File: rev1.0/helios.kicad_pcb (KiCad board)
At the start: 4 copper layers, 17.8 x 33 mm, 58 parts, among them J1 USB_C_Receptacle_USB2.0, J2 helios-pinout, Q1 2N7002VC-, Q2 2N7002VC-, SW1 SWITCH, U1 USBLC6-2P6, U2 LP5907SNX-3.3-NOPB, U3 W25Q128JVPIQ, U4 RP2040, U5 74LVC1T45, Y1 12MHz

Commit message: updated assembly files again
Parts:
- moved R13 0.42 mm to (160.1, 143.8)
- moved R12 0.41 mm to (157.6, 143.8)
- moved JP1 0.28 mm to (153.4, 145.6)
- moved R9 0.20 mm to (155.3, 144.7)
- moved SW1 0.18 mm to (164.5, 161.6)
- moved R11 0.17 mm to (154.8, 146.2)
- moved C16 0.16 mm to (155.5, 150.9)
- moved R2 0.16 mm to (156.8, 143.8)
- moved C10 0.11 mm to (160.4, 150.9)
- moved C14 0.11 mm to (159.3, 150.9)
- moved C17 0.11 mm to (158.4, 150.9)
- moved C18 0.11 mm to (162.2, 150.9)
- moved C9 0.11 mm to (161.3, 150.9)
- moved U1 0.08 mm to (158.9, 143.8)
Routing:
- net GND: track 7.69 -> 8.81 mm, vias 38 -> 39
- net /23_SDO: track 8.66 -> 9.75 mm, vias 0 -> 1
- net /D-: track 12.0 -> 12.6 mm
- net /D+: track 12.0 -> 12.6 mm
- net /1_RX0: track 16.4 -> 16.3 mm, vias 1 -> 0

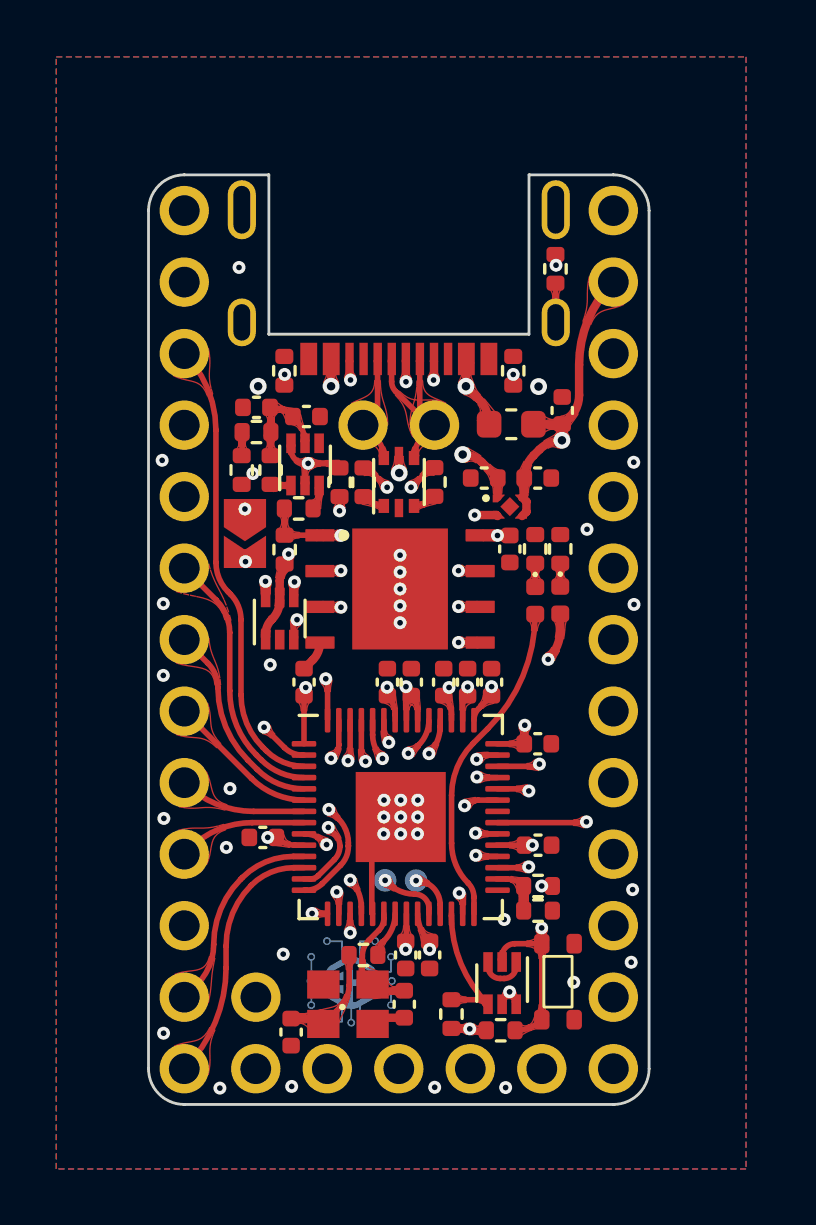
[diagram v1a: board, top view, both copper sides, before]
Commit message: fixed proto mistakes, revised power circuit and added option to use vbus on the 5v pin
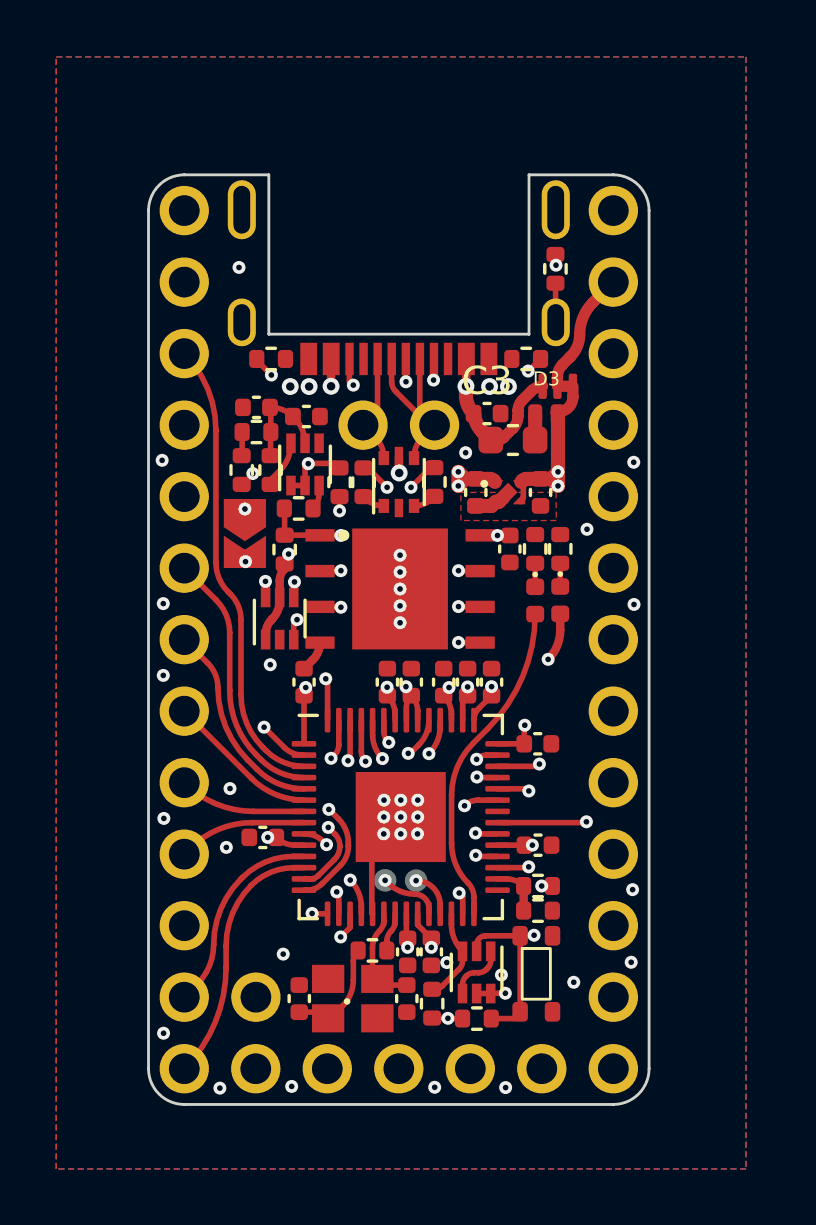
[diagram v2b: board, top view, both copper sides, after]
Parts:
- removed the REF** at (158.8, 160.0)
- added D3: PMEG2010BELD, 0xcb:SOD882D, F.Cu at (164.1, 141.4)
- added JP2: Jumper_3_Bridged12, 0xcb:SolderJumper-3_P1.3mm_Bridged12_RoundedPad1.0x1.5mm_NumberLabels, F.Cu at (164.5, 140.4)
- U2: value LP5907SNX-3.3-NOPB -> TLV75533PDQNR
- moved C3 2.67 mm to (162.0, 141.4), turned to 0 degrees
- moved C8 1.22 mm to (155.3, 162.2), turned to -90 degrees
- moved Q1 0.98 mm to (161.6, 161.2)
- moved R1 0.94 mm to (161.6, 162.9)
- moved SW1 0.82 mm to (163.7, 161.3)
- moved R3 0.78 mm to (160.0, 162.3)
- moved R8 0.63 mm to (154.3, 139.4), turned to 180 degrees
- moved R7 0.62 mm to (163.4, 139.4), turned to 0 degrees
- moved C5 0.59 mm to (161.6, 144.2), turned to -90 degrees
- moved F1 0.56 mm to (162.9, 142.3)
- moved C4 0.52 mm to (163.9, 144.2), turned to -90 degrees
- moved U2 0.51 mm to (162.7, 144.2)
- moved R14 0.36 mm to (157.9, 160.4)
- moved Y1 0.26 mm to (157.2, 162.2)
- moved C7 0.22 mm to (159.1, 162.2)
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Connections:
- C3 pad 1: +5V -> VBUS
- F1 pad 2: +5V -> Net-(D3-Pad2)
- J2 pad 30: +5V -> /RAW
- Q1 pad 3: GND -> /RST
- Q1 pad 4: /RST -> GND
- Q2 pad 1: Net-(Q2-Pad1) -> Net-(Q1-Pad5)
- Q2 pad 6: Net-(Q1-Pad5) -> Net-(Q2-Pad6)
- R4 pad 1: Net-(Q2-Pad1) -> Net-(Q2-Pad6)
- U2 pad 5: unconnected-(U2-Pad5) -> GND
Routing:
- net /RAW: track 0.00 -> 4.36 mm
- net +5V: track 25.0 -> 20.9 mm, vias 3 -> 4
- net VBUS: track 28.5 -> 32.0 mm
- net Net-(Q1-Pad5): track 28.3 -> 26.5 mm
- net Net-(Q2-Pad6): track 0.00 -> 1.69 mm
- net /RST: track 4.88 -> 3.33 mm
- net Net-(J1-PadB5): track 3.61 -> 4.91 mm
- net Net-(D3-Pad2): track 0.00 -> 0.92 mm
- net Net-(Q2-Pad1): track 0.74 -> 0.00 mm
- net Net-(J1-PadA5): track 4.09 -> 4.82 mm
- net GND: track 8.81 -> 8.22 mm, vias 39 -> 42
- net Net-(C7-Pad2): track 4.10 -> 3.60 mm
- net +3V3: track 20.5 -> 20.6 mm, vias 15 -> 16

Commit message: prod files
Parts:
- added REF**: LOGO, art:LOGO, B.Cu at (158.9, 162.2)
- moved D2 2.97 mm to (163.0, 150.9)
- moved D1 2.97 mm to (163.9, 150.9)
- moved R10 2.97 mm to (163.9, 149.1)
- moved R15 2.97 mm to (163.0, 149.1)
- moved C6 0.83 mm to (163.5, 145.7), turned to 0 degrees
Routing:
- net /LED: track 11.7 -> 8.77 mm
- net Net-(D1-Pad2): track 24.1 -> 22.3 mm
- net +3V3: track 20.6 -> 21.3 mm, vias 16 -> 15
- net GND: vias 42 -> 45

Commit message: production files
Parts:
- C1, C10, C11, C12, C13, C14, C15, C16, C17, C18, C19, C2, C3, C4, C5, C6, C7, C8, C9: footprint Capacitor_SMD:C_0402_1005Metric -> 0xcb:C_0402_1005Metric
- D1, D2: footprint Diode_SMD:D_0402_1005Metric -> 0xcb:D_0402_1005Metric
- F1: footprint Fuse:Fuse_0603_1608Metric -> 0xcb:Fuse_0603_1608Metric
- FB1, R1, R10, R11, R12, R13, R14, R15, R16, R17, R2, R3, R4, R5, R6, R7, R8, R9: footprint Resistor_SMD:R_0402_1005Metric -> 0xcb:R_0402_1005Metric
- Q1, Q2, U5: footprint Package_TO_SOT_SMD:SOT-563 -> 0xcb:SOT-563
- U1: footprint Package_TO_SOT_SMD:SOT-666 -> 0xcb:SOT-666
- U4: footprint Package_DFN_QFN:QFN-56-1EP_7x7mm_P0.4mm_EP3.2x3.2mm -> 0xcb:QFN-56-1EP_7x7mm_P0.4mm_EP3.2x3.2mm
- Y1: footprint Crystal:Crystal_SMD_2520-4Pin_2.5x2.0mm -> 0xcb:Crystal_SMD_2520-4Pin_2.5x2.0mm

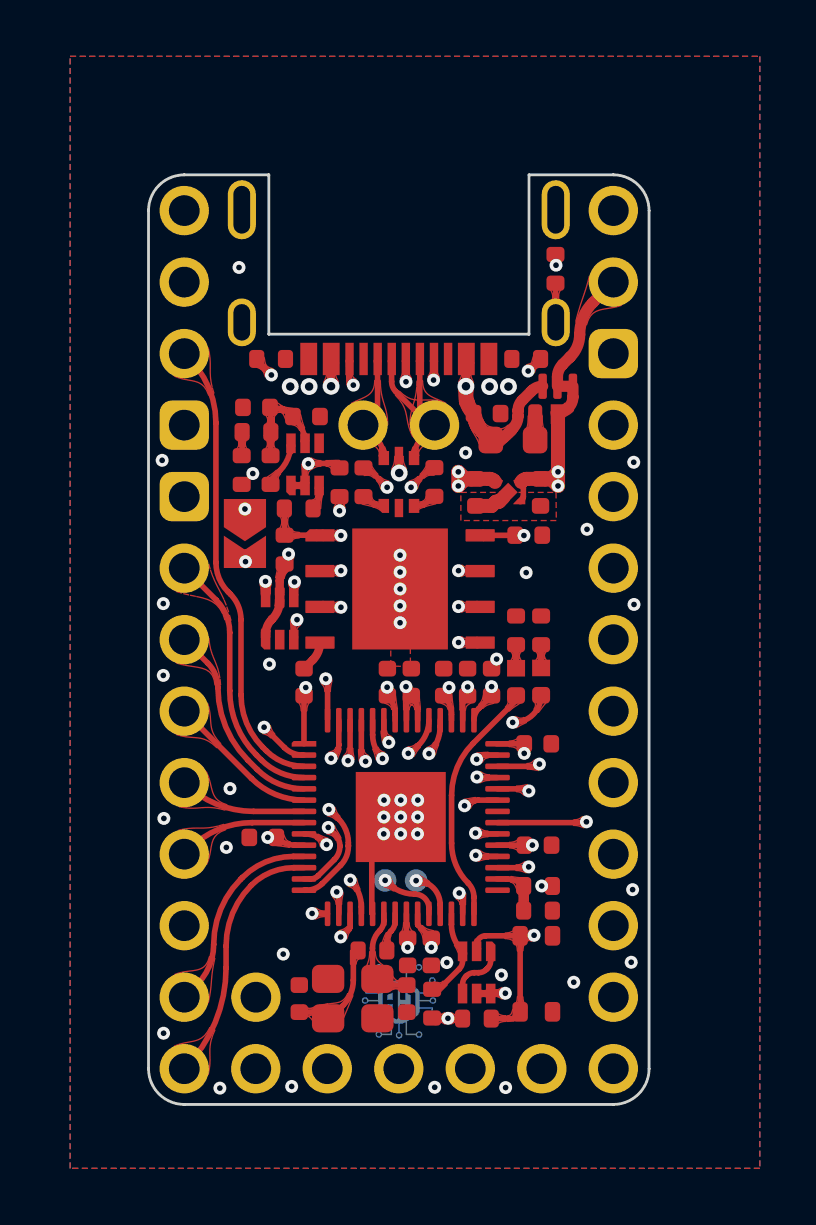
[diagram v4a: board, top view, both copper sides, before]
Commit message: add castellated holes
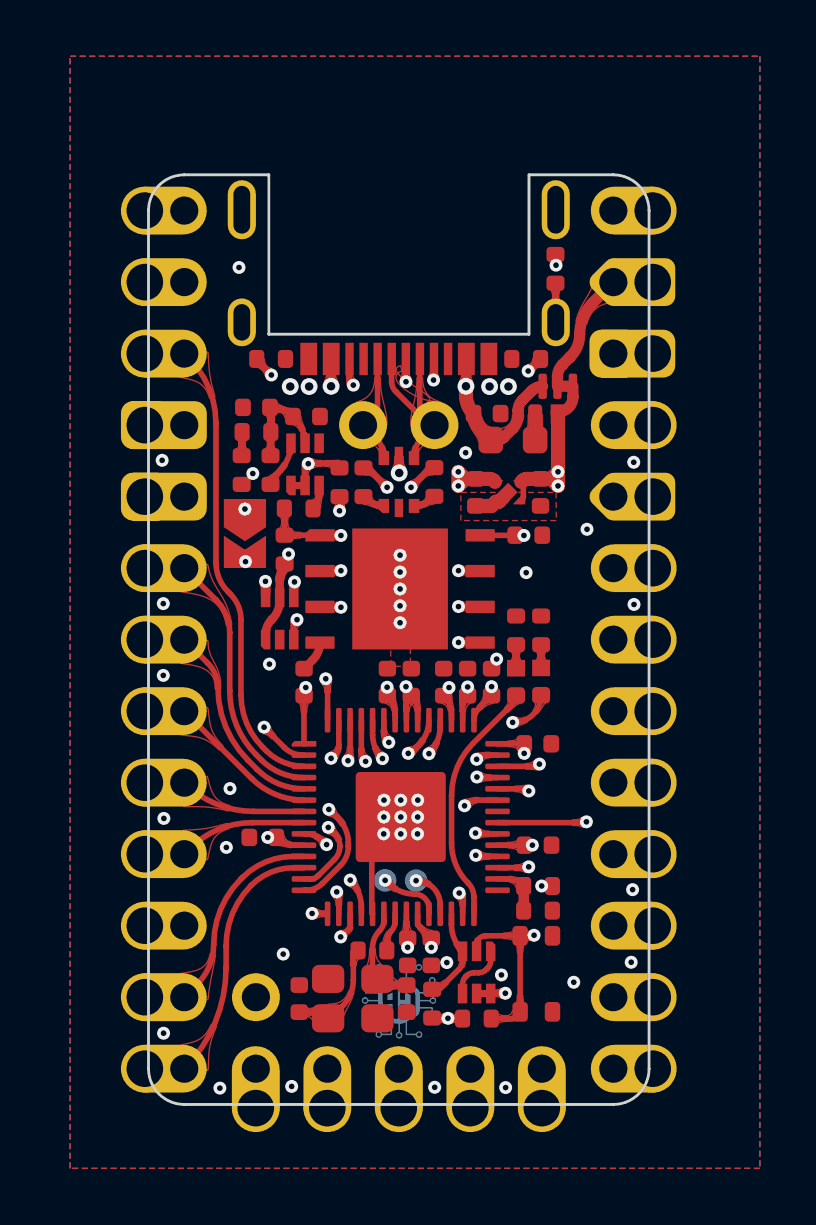
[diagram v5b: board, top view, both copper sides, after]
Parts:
- U4: footprint 0xcb:QFN-56-1EP_7x7mm_P0.4mm_EP3.2x3.2mm -> 0xcb:RP2040-QFN-56

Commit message: fix tabs in pads
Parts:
- removed the REF** at (158.9, 166.3)
- added REF**: Tab, kikit:Tab, F.Cu at (165.7, 166.4)
- added REF**: Tab, kikit:Tab, F.Cu at (152.0, 166.4)
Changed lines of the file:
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@@
+      (stroke (width 0.3) (type solid)) (layer "Dwgs.User"))
+  )
+  (footprint "kikit:Tab" (layer "F.Cu")
+    (at 165.73 166.36 90)
+    (descr "A symbol representing annotation for tab placement")
+    (attr board_only exclude_from_pos_files exclude_from_bom)
+    (fp_text reference "REF**" (at 0 -2 90) (layer "F.SilkS") hide
+        (effects (font (size 1 1) (thickness 0.15)))
+    )
+    (fp_text value "Tab" (at -2.75 -1 90) (layer "Dwgs.User")
+        (effects (font (size 1.2 1.2) (thickness 0.2)))
+    )
+    (fp_text user "KIKIT: width: 1.5mm" (at -5.5 0) (layer "Dwgs.User")
+        (effects (font (size 1 1) (thickness 0.15)))
+    )
+    (fp_line (start 0.25 0) (end -2.75 0)
+      (stroke (width 0.3) (type solid)) (layer "Dwgs.User"))
+    (fp_line (start 0.25 0) (end -0.75 -1)
+      (stroke (width 0.3) (type solid)) (layer "Dwgs.User"))
+    (fp_line (start 0.25 0) (end -0.75 1)
+      (stroke (width 0.3) (type solid)) (layer "Dwgs.User"))
+    (fp_line (start 0.25 1) (end 0.25 -1)
       (stroke (width 0.3) (type solid)) (layer "Dwgs.User"))
   )
@@
       (rotate (xyz 0 0 0))
     )
-  )
-  (footprint "kikit:Tab" (layer "F.Cu")
-    (at 158.9 166.26 90)
-    (descr "A symbol representing annotation for tab placement")
-    (attr board_only exclude_from_pos_files exclude_from_bom)
-    (fp_text reference "REF**" (at 0 -2 90) (layer "F.SilkS") hide
-        (effects (font (size 1 1) (thickness 0.15)))
-    )
-    (fp_text value "Tab" (at -2.75 -1 90) (layer "Dwgs.User")
-        (effects (font (size 1.2 1.2) (thickness 0.2)))
-    )
-    (fp_text user "KIKIT: width: 6mm" (at -5.5 0) (layer "Dwgs.User")
-        (effects (font (size 1 1) (thickness 0.15)))
-    )
-    (fp_line (start 0.25 0) (end -2.75 0)
-      (stroke (width 0.3) (type solid)) (layer "Dwgs.User"))
-    (fp_line (start 0.25 0) (end -0.75 -1)
-      (stroke (width 0.3) (type solid)) (layer "Dwgs.User"))
-    (fp_line (start 0.25 0) (end -0.75 1)
-      (stroke (width 0.3) (type solid)) (layer "Dwgs.User"))
-    (fp_line (start 0.25 1) (end 0.25 -1)
-      (stroke (width 0.3) (type solid)) (layer "Dwgs.User"))
   )
   (footprint "0xcb:C_0402_1005Metric" (layer "F.Cu")
@@
     )
   )
+  (footprint "kikit:Tab" (layer "F.Cu")
+    (at 151.98 166.36 90)
+    (descr "A symbol representing annotation for tab placement")
+    (attr board_only exclude_from_pos_files exclude_from_bom)
+    (fp_text reference "REF**" (at 0 -2 90) (layer "F.SilkS") hide
+        (effects (font (size 1 1) (thickness 0.15)))
+    )
+    (fp_text value "Tab" (at -2.75 -1 90) (layer "Dwgs.User")
+        (effects (font (size 1.2 1.2) (thickness 0.2)))
+    )
+    (fp_text user "KIKIT: width: 1.5mm" (at -5.5 0) (layer "Dwgs.User")
+        (effects (font (size 1 1) (thickness 0.15)))
+    )
+    (fp_line (start 0.25 0) (end -2.75 0)
+      (stroke (width 0.3) (type solid)) (layer "Dwgs.User"))
+    (fp_line (start 0.25 0) (end -0.75 -1)
+      (stroke (width 0.3) (type solid)) (layer "Dwgs.User"))
+    (fp_line (start 0.25 0) (end -0.75 1)
+      (stroke (width 0.3) (type solid)) (layer "Dwgs.User"))
+    (fp_line (start 0.25 1) (end 0.25 -1)
+      (stroke (width 0.3) (type solid)) (layer "Dwgs.User"))
+  )
   (footprint "0xcb:C_0402_1005Metric" (layer "F.Cu")
